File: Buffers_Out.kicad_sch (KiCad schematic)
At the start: 35 parts, among them J2 NMJ6HCD2, U6 NE5532, U7 NE5532

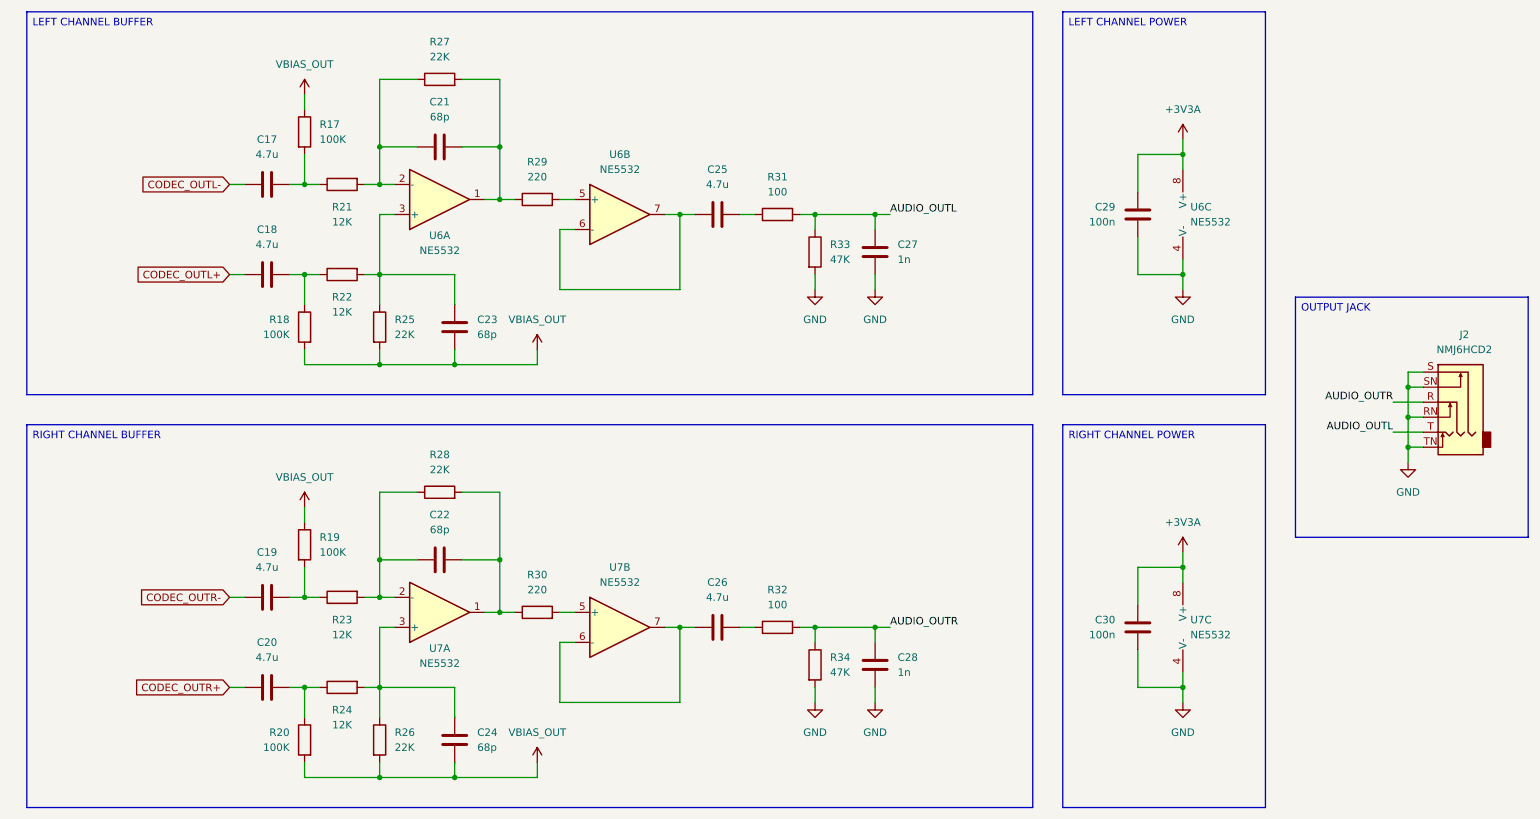
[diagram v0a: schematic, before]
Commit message: Schematic
Updated the schematic.
Added the codec schematic module.
Added the buffer schematic module.
Added the RP2350 schematic module.
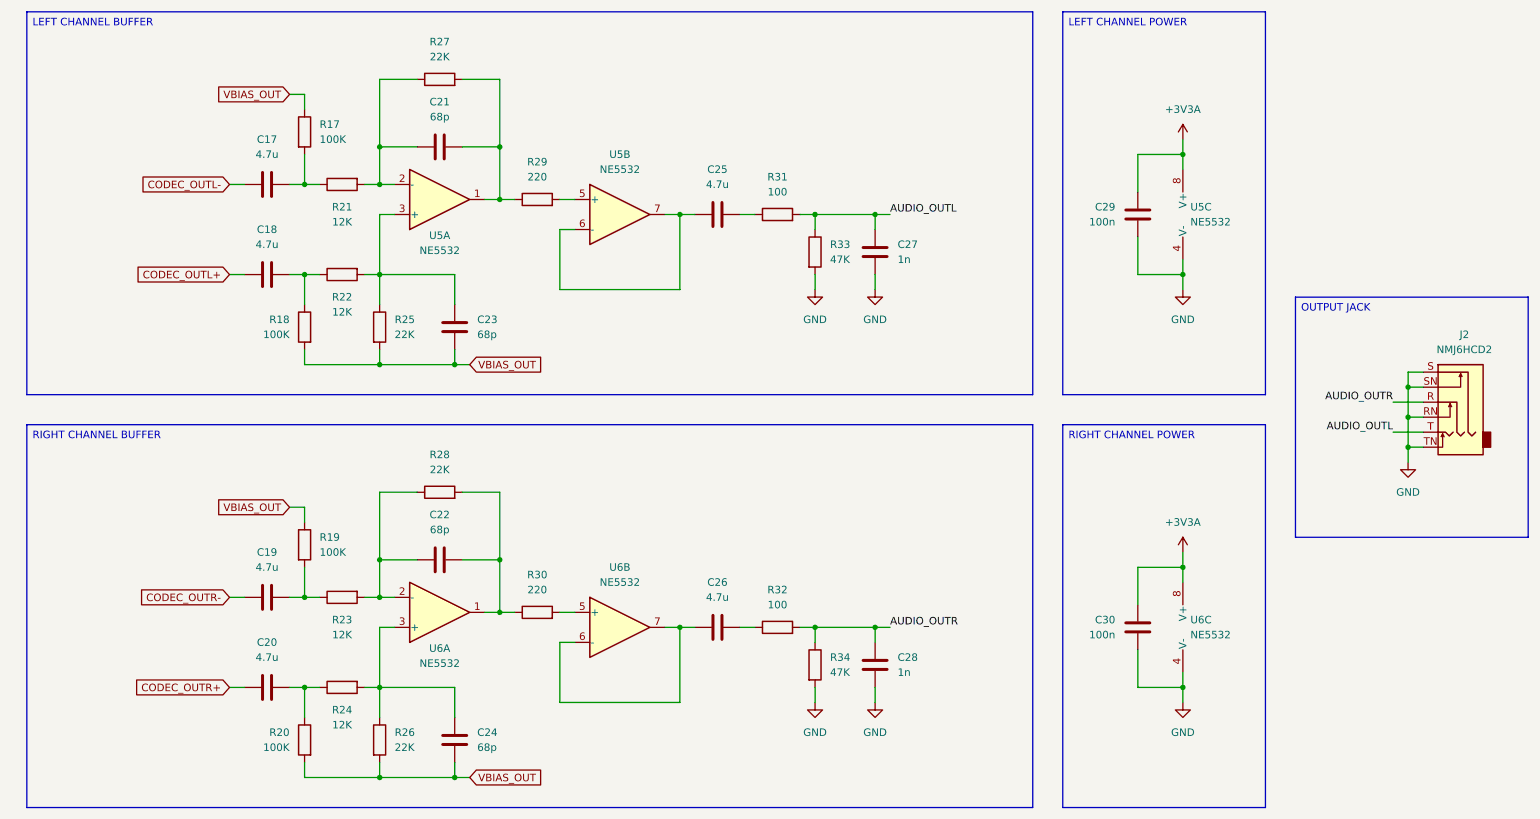
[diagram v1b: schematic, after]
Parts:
- C17, C18, C19, C20, C25, C26: footprint (none) -> Capacitor_SMD:C_1206_3216Metric
- C21, C22, C23, C24, C27, C28: footprint (none) -> Capacitor_SMD:C_0603_1608Metric
- renumbered U6 to U5, U7 to U6

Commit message: Schematic
Updated the power delivery module.
Other minor changes.
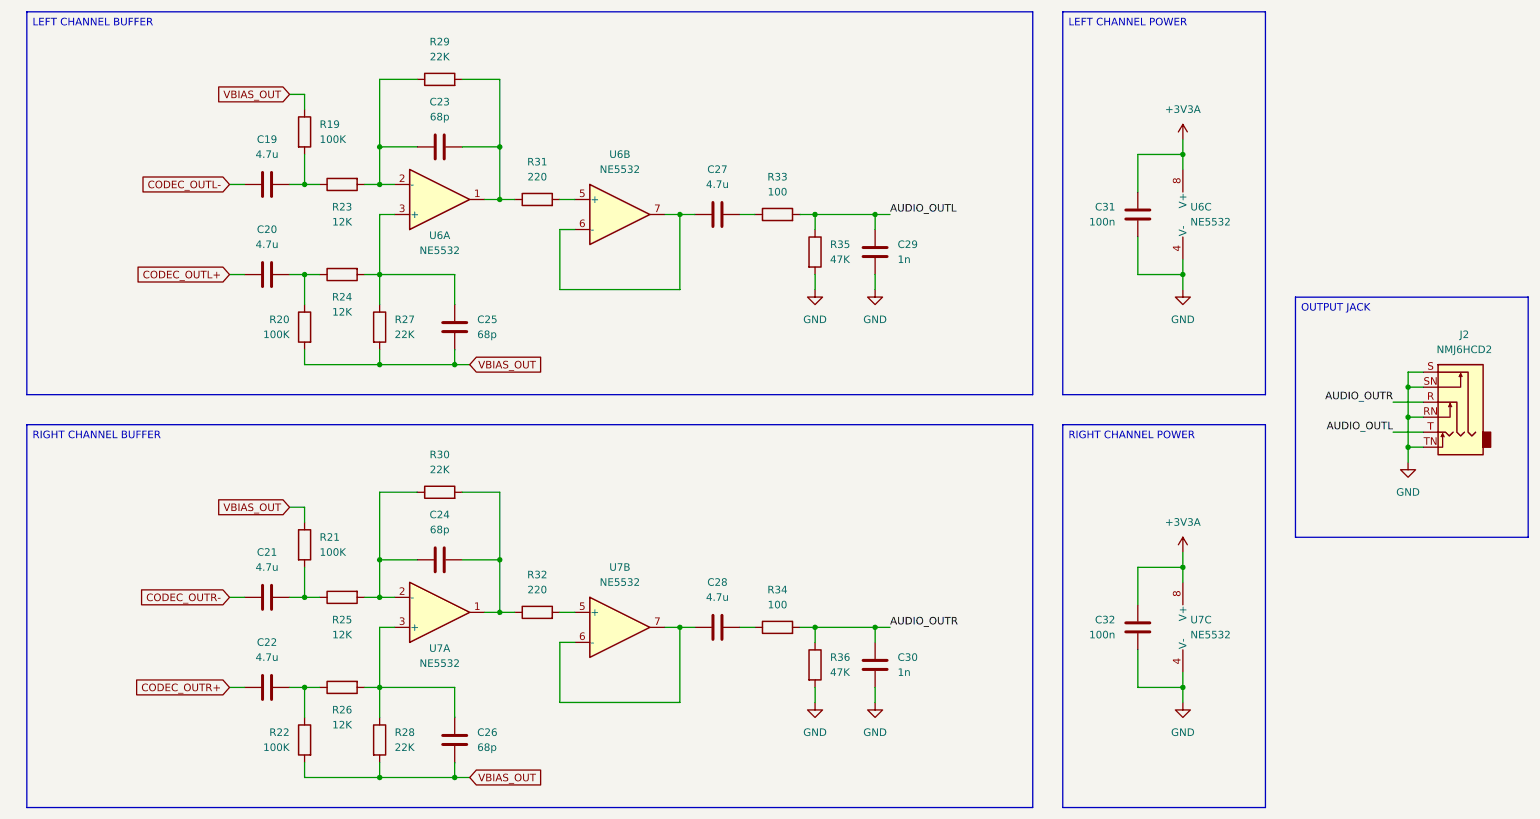
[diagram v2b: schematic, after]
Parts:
- renumbered C17 to C19, C18 to C20, C19 to C21, C20 to C22, C21 to C23, C22 to C24, C23 to C25, C24 to C26, C25 to C27, C26 to C28, C27 to C29, C28 to C30, C29 to C31, C30 to C32, R17 to R19, R18 to R20, R19 to R21, R20 to R22, R21 to R23, R22 to R24, R23 to R25, R24 to R26, R25 to R27, R26 to R28, R27 to R29, R28 to R30, R29 to R31, R30 to R32, R31 to R33, R32 to R34, R33 to R35, R34 to R36, U5 to U6, U6 to U7
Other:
- company: (none) -> DavidMolTor
- title: (none) -> SIMPLE CODEC

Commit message: Moved to a CS4272 codec as a cheaper alternative with similar performance.
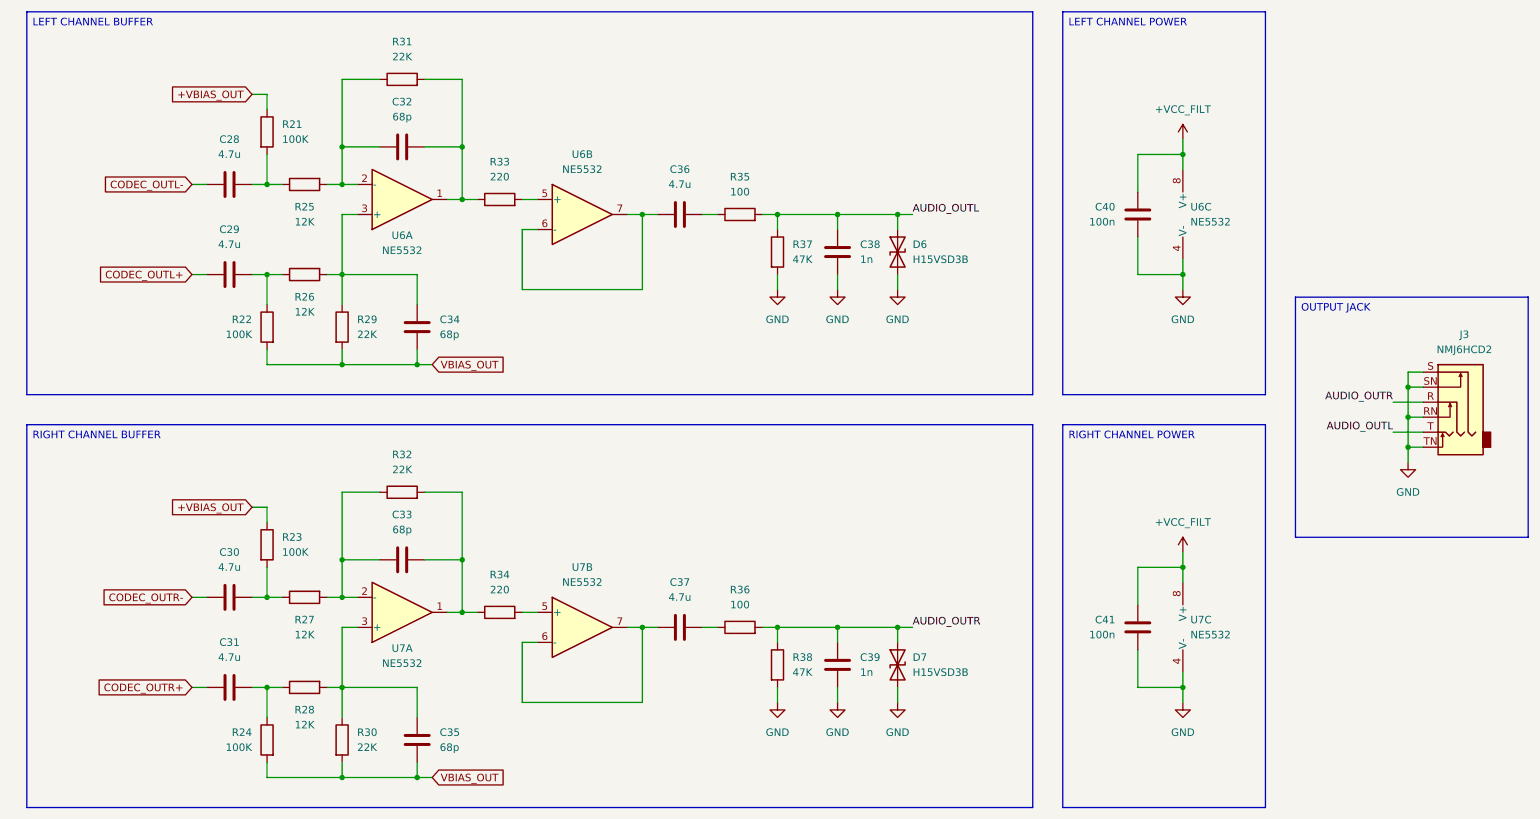
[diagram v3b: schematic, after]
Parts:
- added D6, D7: H15VSD3B, Diode_SMD:D_SOD-323, symbol Device:D_TVS
- renumbered C19 to C28, C20 to C29, C21 to C30, C22 to C31, C23 to C32, C24 to C33, C25 to C34, C26 to C35, C27 to C36, C28 to C37, C29 to C38, C30 to C39, C31 to C40, C32 to C41, J2 to J3, R19 to R21, R20 to R22, R21 to R23, R22 to R24, R23 to R25, R24 to R26, R25 to R27, R26 to R28, R27 to R29, R28 to R30, R29 to R31, R30 to R32, R31 to R33, R32 to R34, R33 to R35, R34 to R36, R35 to R37, R36 to R38
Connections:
- net AUDIO_OUTL: now also D6.1 (A1)
- net AUDIO_OUTR: now also D7.1 (A1)
- net GND: now also D6.2 (A2), D7.2 (A2)
- net VBIAS_OUT: no longer R21.1, R23.1
- net +3V3A renamed +VCC_FILT
- new net +VBIAS_OUT: R21.1, R23.1
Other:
- moved on the sheet: C28, C29, C30, C31, C32, C33, C34, C35, C36, C37, C38, C39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

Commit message: Initial layout
Initial layout inside a 1590N1/125B pedal enclosure.
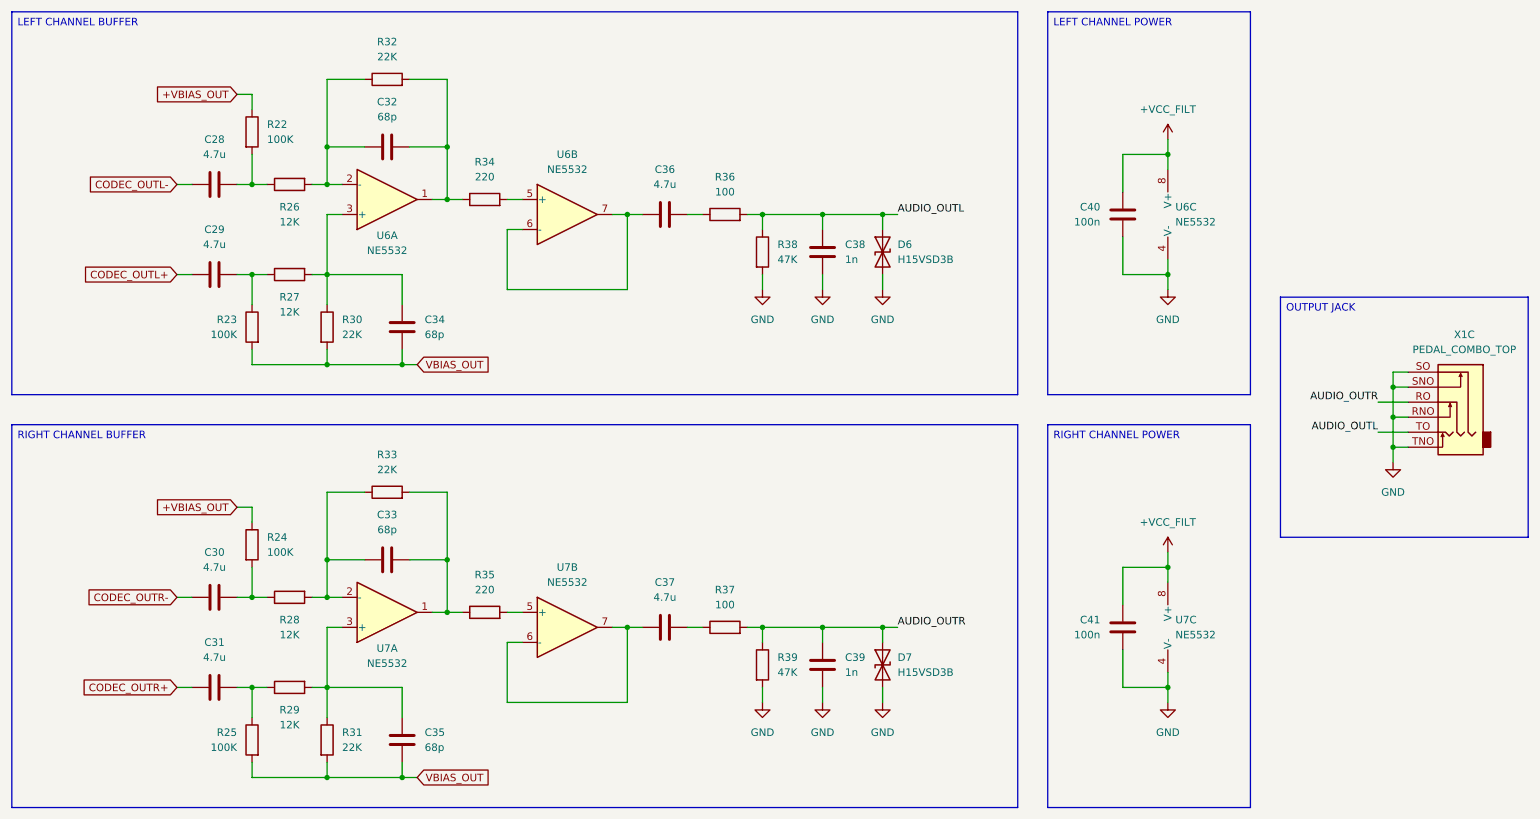
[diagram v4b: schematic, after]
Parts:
- removed J3: NMJ6HCD2, Custom_Parts:NMJ6HCD2_BORDER, symbol Connector_Audio:NMJ6HCD2
- added X1: PEDAL_COMBO_TOP, Custom_Parts:PEDAL_COMBO_TOP, symbol Custom_Parts:PEDAL_COMBO_TOP
- renumbered R21 to R22, R22 to R23, R23 to R24, R24 to R25, R25 to R26, R26 to R27, R27 to R28, R28 to R29, R29 to R30, R30 to R31, R31 to R32, R32 to R33, R33 to R34, R34 to R35, R35 to R36, R36 to R37, R37 to R38, R38 to R39
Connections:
- net AUDIO_OUTL: now also X1.TO
- net AUDIO_OUTR: now also X1.RO
- net GND: now also X1.RNO, X1.SNO, X1.SO, X1.TNO
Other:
- moved on the sheet: C28, C29, C30, C31, C32, C33, C34, C35, C36, C37, C38, C39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
